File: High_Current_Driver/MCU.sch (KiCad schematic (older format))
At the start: 13 parts, among them J9 Conn_01x02

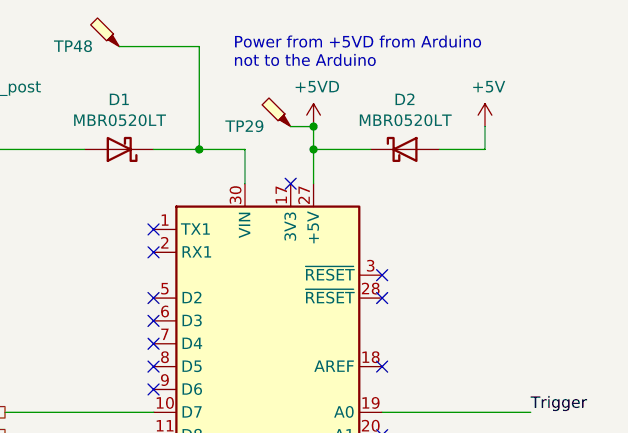
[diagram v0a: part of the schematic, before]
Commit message: HCD amplifier update
-Updated OPA2277 amplifiers to OPA2210 that were actually populated on the boards
-Added DNP to one of the power mux diodes
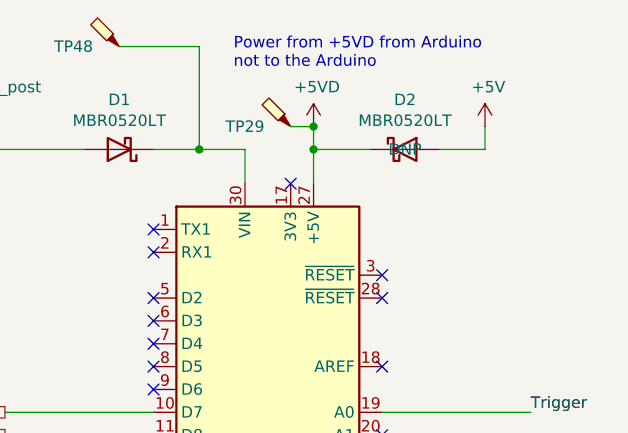
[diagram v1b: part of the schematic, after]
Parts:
- D2: DNP (none) -> DNP
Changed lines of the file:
@@
 F 2 "Diode_SMD:D_SOD-123" H 6450 2475 50  0001 C CNN
 F 3 "http://www.onsemi.com/pub_link/Collateral/MBR0520LT1-D.PDF" H 6450 2650 50  0001 C CNN
+F 4 "DNP" H 6450 2650 50  0000 C CNN "DNP"
 	1    6450 2650
 	1    0    0    -1

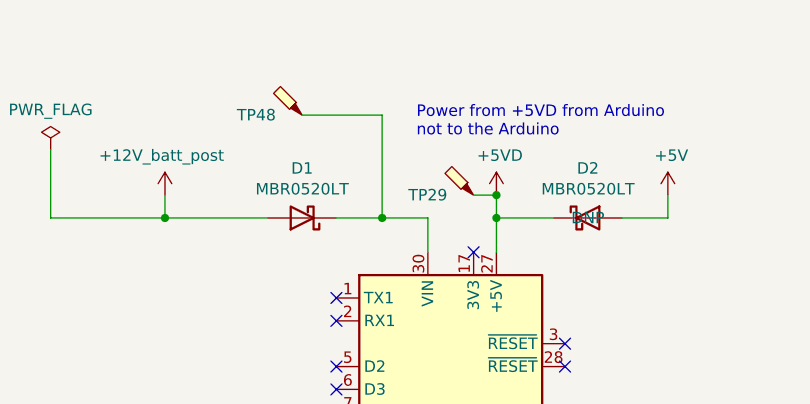
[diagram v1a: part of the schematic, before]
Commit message: HCD missing power flag on MCU fix
Added the missing power flag that was on the diode power mux
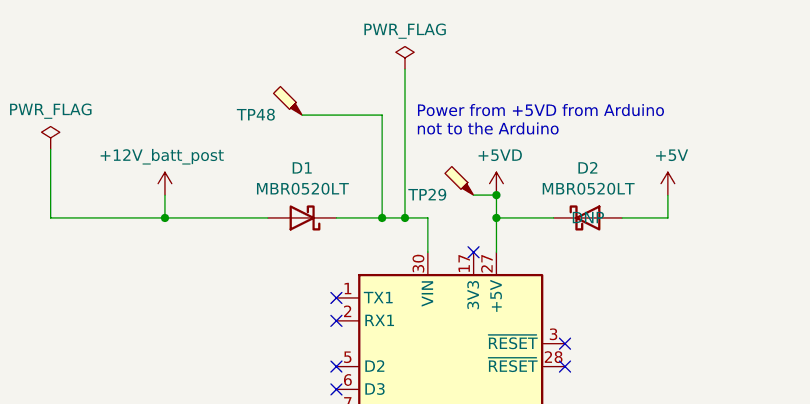
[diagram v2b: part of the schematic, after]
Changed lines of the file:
@@
 Connection ~ 4600 2650
 Wire Wire Line
-	5750 2650 5550 2650
+	5750 2650 5650 2650
 Wire Wire Line
 	5550 2200 5550 2650
@@
 Trigger output for calibration
 NoConn ~ 5350 3700
+$Comp
+L power:PWR_FLAG #FLG0108
+U 1 1 629DFF21
+P 5650 2000
+F 0 "#FLG0108" H 5650 2075 50  0001 C CNN
+F 1 "PWR_FLAG" H 5650 2173 50  0000 C CNN
+F 2 "" H 5650 2000 50  0001 C CNN
+F 3 "~" H 5650 2000 50  0001 C CNN
+	1    5650 2000
+	1    0    0    -1
+$EndComp
+Wire Wire Line
+	5650 2000 5650 2650
+Connection ~ 5650 2650
+Wire Wire Line
+	5650 2650 5550 2650
 $EndSCHEMATC
